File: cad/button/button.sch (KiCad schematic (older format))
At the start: 17 parts, among them J1 uSD_SPI, J2 SWD, SW1 SW_Push, U1 STM32L072KZTx, U2 PAM8302AAS

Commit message: more drawing
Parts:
- J1: footprint Connectors:microSD_Card_Receptacle_Wuerth_693072010801 -> custom:PJRC_uSD_Adapter
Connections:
- wire segments 59 -> 53
- no-connect marks 17 -> 16
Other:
- moved on the sheet: J1, J2
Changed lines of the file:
@@
 NoConn ~ 3250 3600
 NoConn ~ 3250 3700
-NoConn ~ 3250 4000
 NoConn ~ 2150 3100
 NoConn ~ 2150 3200
@@
 L Connector:Conn_01x04_Female J2
 U 1 1 5C3A9A62
-P 4100 4050
-F 0 "J2" H 4128 4026 50  0000 L CNN
-F 1 "SWD" H 4128 3935 50  0000 L CNN
-F 2 "custom:Pad_4contacts" H 4100 4050 50  0001 C CNN
-F 3 "~" H 4100 4050 50  0001 C CNN
-	1    4100 4050
+P 4100 3800
+F 0 "J2" H 4128 3776 50  0000 L CNN
+F 1 "SWD" H 4128 3685 50  0000 L CNN
+F 2 "custom:Pad_4contacts" H 4100 3800 50  0001 C CNN
+F 3 "~" H 4100 3800 50  0001 C CNN
+	1    4100 3800
 	1    0    0    -1
 $EndComp
@@
 L power:GND #PWR0101
 U 1 1 5C3AA417
-P 3900 4300
-F 0 "#PWR0101" H 3900 4050 50  0001 C CNN
-F 1 "GND" H 3905 4127 50  0000 C CNN
-F 2 "" H 3900 4300 50  0001 C CNN
-F 3 "" H 3900 4300 50  0001 C CNN
-	1    3900 4300
+P 3900 4050
+F 0 "#PWR0101" H 3900 3800 50  0001 C CNN
+F 1 "GND" H 3905 3877 50  0000 C CNN
+F 2 "" H 3900 4050 50  0001 C CNN
+F 3 "" H 3900 4050 50  0001 C CNN
+	1    3900 4050
 	1    0    0    -1
 $EndComp
@@
 L power:+3V3 #PWR0106
 U 1 1 5C3AA5DA
-P 3900 3900
-F 0 "#PWR0106" H 3900 3750 50  0001 C CNN
-F 1 "+3V3" H 3915 4073 50  0000 C CNN
-F 2 "" H 3900 3900 50  0001 C CNN
-F 3 "" H 3900 3900 50  0001 C CNN
-	1    3900 3900
+P 3900 3650
+F 0 "#PWR0106" H 3900 3500 50  0001 C CNN
+F 1 "+3V3" H 3915 3823 50  0000 C CNN
+F 2 "" H 3900 3650 50  0001 C CNN
+F 3 "" H 3900 3650 50  0001 C CNN
+	1    3900 3650
 	1    0    0    -1
 $EndComp
@@
 Text Label 1850 2700 0    50   ~ 0
 BOOT0
-Wire Wire Line
-	3250 3800 3600 3800
-Wire Wire Line
-	3250 3900 3550 3900
 $Comp
 L custom:uSD_SPI J1
 U 1 1 5C3DB7D2
-P 5950 3900
-F 0 "J1" H 5900 4617 50  0000 C CNN
-F 1 "uSD_SPI" H 5900 4526 50  0000 C CNN
-F 2 "Connectors:microSD_Card_Receptacle_Wuerth_693072010801" H 7100 4200 50  0001 C CNN
-F 3 "http://katalog.we-online.de/em/datasheet/693072010801.pdf" H 5950 3900 50  0001 C CNN
-	1    5950 3900
+P 5950 4150
+F 0 "J1" H 5900 4867 50  0000 C CNN
+F 1 "uSD_SPI" H 5900 4776 50  0000 C CNN
+F 2 "custom:PJRC_uSD_Adapter" H 7100 4450 50  0001 C CNN
+F 3 "http://katalog.we-online.de/em/datasheet/693072010801.pdf" H 5950 4150 50  0001 C CNN
+	1    5950 4150
 	1    0    0    -1
 $EndComp
@@
 Text GLabel 3250 2900 2    50   Input ~ 0
 SPK_IN
-Text GLabel 3250 3300 2    50   Input ~ 0
+Text GLabel 3250 4000 2    50   Input ~ 0
 SPK_SD
 Text GLabel 5100 2250 0    50   Input ~ 0
 SPK_IN
-Text GLabel 5050 3700 0    50   Input ~ 0
+Text GLabel 5050 4000 0    50   Input ~ 0
 SD_CS
-Text GLabel 5050 4000 0    50   Input ~ 0
+Text GLabel 5050 4100 0    50   Input ~ 0
 SD_SCK
+Text GLabel 5050 4300 0    50   Input ~ 0
+SD_MISO
 Text GLabel 5050 4200 0    50   Input ~ 0
-SD_MISO
-Text GLabel 5050 3800 0    50   Input ~ 0
 SD_MOSI
-Wire Wire Line
-	5050 3900 4550 3900
-Wire Wire Line
-	4550 3900 4550 3800
-Wire Wire Line
-	5050 4100 4550 4100
 $Comp
 L power:GND #PWR0115
 U 1 1 5C3DDAEF
-P 4550 4300
-F 0 "#PWR0115" H 4550 4050 50  0001 C CNN
-F 1 "GND" H 4555 4127 50  0000 C CNN
-F 2 "" H 4550 4300 50  0001 C CNN
-F 3 "" H 4550 4300 50  0001 C CNN
-	1    4550 4300
+P 5500 4900
+F 0 "#PWR0115" H 5500 4650 50  0001 C CNN
+F 1 "GND" H 5505 4727 50  0000 C CNN
+F 2 "" H 5500 4900 50  0001 C CNN
+F 3 "" H 5500 4900 50  0001 C CNN
+	1    5500 4900
 	1    0    0    -1
 $EndComp
@@
 L power:+3V3 #PWR0116
 U 1 1 5C3DDB14
-P 4550 3800
-F 0 "#PWR0116" H 4550 3650 50  0001 C CNN
-F 1 "+3V3" H 4565 3973 50  0000 C CNN
-F 2 "" H 4550 3800 50  0001 C CNN
-F 3 "" H 4550 3800 50  0001 C CNN
-	1    4550 3800
-	1    0    0    -1
-$EndComp
-NoConn ~ 6750 4500
+P 5500 3450
+F 0 "#PWR0116" H 5500 3300 50  0001 C CNN
+F 1 "+3V3" H 5515 3623 50  0000 C CNN
+F 2 "" H 5500 3450 50  0001 C CNN
+F 3 "" H 5500 3450 50  0001 C CNN
+	1    5500 3450
+	1    0    0    -1
+$EndComp
 Wire Wire Line
 	1450 2700 1450 2750
@@
 	2650 4250 2650 4300
 Wire Wire Line
-	3900 3900 3900 3950
-Wire Wire Line
-	3900 4250 3900 4300
-Wire Wire Line
-	3900 4150 3550 4150
-Wire Wire Line
-	3550 3900 3550 4150
-Wire Wire Line
-	3900 4050 3600 4050
-Wire Wire Line
-	3600 3800 3600 4050
-Wire Wire Line
-	4550 4100 4550 4300
+	3900 3650 3900 3700
+Wire Wire Line
+	3900 4000 3900 4050
+Wire Wire Line
+	5500 3450 5500 3500
+Wire Wire Line
+	5500 4850 5500 4900
+NoConn ~ 3250 3300
+Wire Wire Line
+	3250 3900 3900 3900
+Wire Wire Line
+	3250 3800 3900 3800
 $EndSCHEMATC

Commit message: finish up schematic
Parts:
- removed C2: 1uF, Capacitors_SMD:C_0603_HandSoldering, symbol Device:CP_Small
- removed C3: 10uF, Capacitors_SMD:C_0603_HandSoldering, symbol Device:CP_Small
- removed C6: 100nF, Capacitors_SMD:C_0603_HandSoldering, symbol Device:C_Small
- added C1, C2, C9: 10uF, Capacitors_SMD:C_0603_HandSoldering, symbol Device:C_Small
- added C10, C11: 220pF, Capacitors_SMD:C_0603_HandSoldering, symbol Device:C_Small
- added C5, C7, C8: 1uF, Capacitors_SMD:C_0603_HandSoldering, symbol Device:C_Small
- added FB1, FB2: Ferrite_Bead_Small, Resistors_SMD:R_0603_HandSoldering, symbol Device:Ferrite_Bead_Small
- added Q1: DMC2038LVT, TO_SOT_Packages_SMD:TSOT-23-6, symbol custom:DMC2038LVT
- added R1, R6, R7: 10K, Resistors_SMD:R_0603_HandSoldering, symbol Device:R_Small
- added R4: 10, Resistors_SMD:R_0603_HandSoldering, symbol Device:R_Small
- added RV1: R_POT, Potentiometers:Potentiometer_Trimmer-EVM3E, symbol Device:R_POT
- R2: value 1K -> 10K
- R3: value 10K -> not fitted
- SW1: value SW_Push -> Button
- renumbered C4 to C3, C5 to C4, C1 to C6, R1 to R5, R4 to R8
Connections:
- net +3V3: now also R3.1, R8.1, C2.1, C9.2, Q1.6 (D), R4.1; no longer BT1.1 (+), C6.2, SW1.2, U1.5 (VDDA)
- net GND: now also R2.2, SW1.2, C1.2, C10.2, C11.2, C2.2, C5.1, C9.1, Q1.4 (D); no longer R3.2, R8.1, U2.4 (IN-)
- net SD_CS: now also U1.25 (PA15); no longer U1.14 (PB0)
- net SD_MISO: now also U1.27 (PB4); no longer U1.12 (PA6)
- net SD_MOSI: now also U1.28 (PB5); no longer U1.13 (PA7)
- net SD_SCK: now also U1.26 (PB3); no longer U1.11 (PA5)
- net SPK_SD: now also U1.22 (PA12); no longer U1.25 (PA15)
- net SPK_1: no longer names the net of U2.5 (OUT+)
- net SPK_1: now also FB1.1; no longer LS1.1
- net SPK_2: no longer names the net of U2.8 (OUT-)
- net SPK_2: now also FB2.1; no longer LS1.2
- net SPK_IN: no longer names the net of U2.3 (IN+)
- net SPK_IN: now also R6.1; no longer U1.10 (PA4)
- net SW_IN: no longer names the net of U1.6 (PA0)
- net SW_IN: no longer R2.2
- new net: R7.1, U2.4 (IN-)
- new net: C7.2, RV1.2
- new net: C7.1, R6.2
- new net: C8.1, R7.2
- new net GATE_N: Q1.1 (G), Q1.2 (S), R1.1, SW1.1
- new net GATE_P: Q1.3 (G), R2.1, R3.2
- new net SPK+: C11.1, FB1.2, LS1.1
- new net SPK-: C10.1, FB2.2, LS1.2
- new net SPK_IN+: RV1.3, U1.10 (PA4)
- new net SPK_IN-: C8.2, RV1.1, U1.11 (PA5)
- new net VBAT: BT1.1 (+), C1.1, Q1.5 (S), R1.2
- new net VDDA: C5.2, C6.2, R4.2, U1.5 (VDDA)
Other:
- note added: "Audio amplifier"
- note added: "Battery and power-on switch"
- note added: "MCU and programming header"
- note added: "SD card adapter"
- moved on the sheet: BT1, C3, C4, C6, J1, J2, LS1, R5, R8, SW1, U1, U2

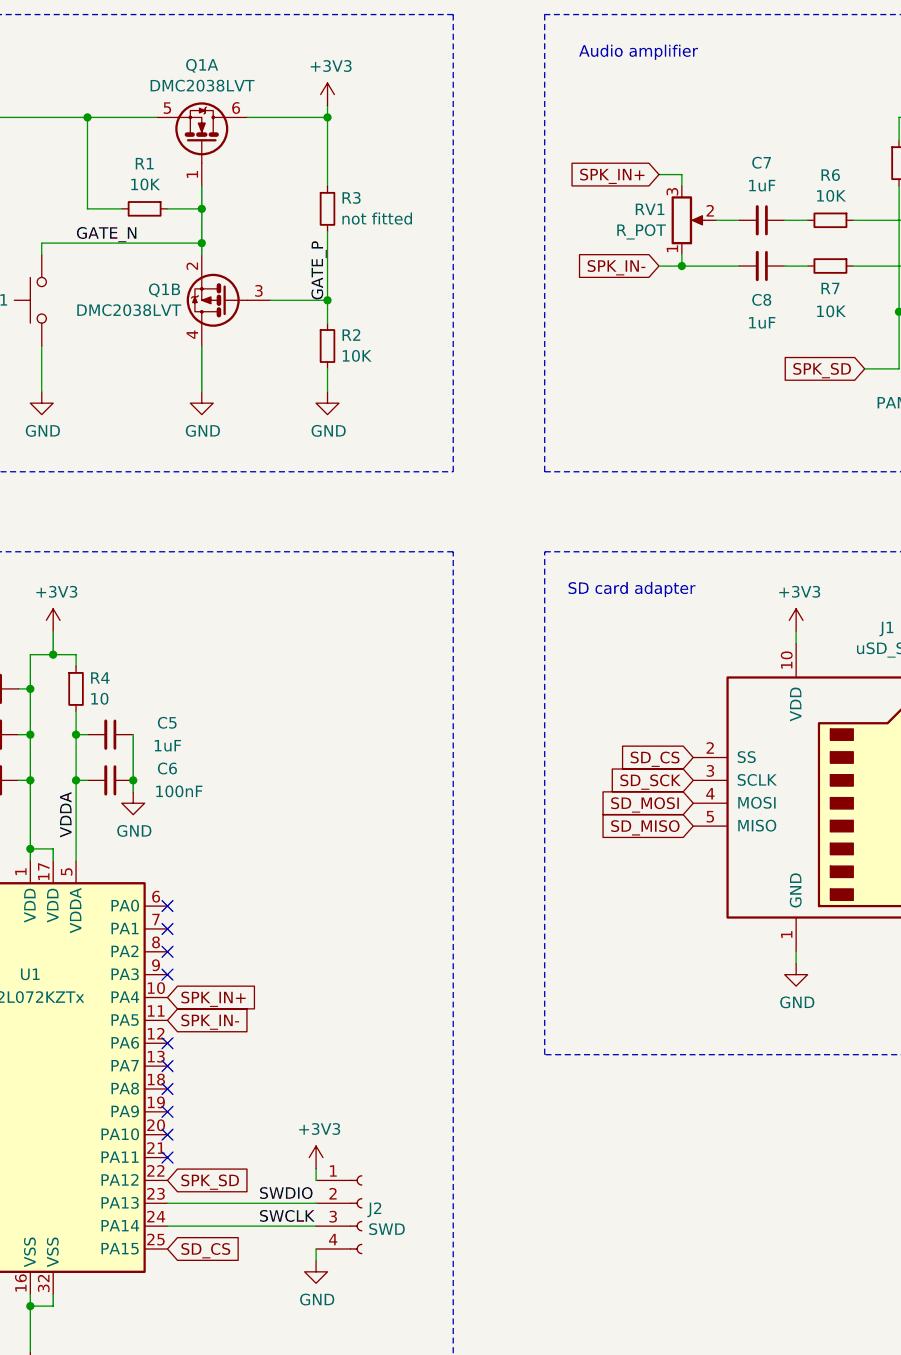
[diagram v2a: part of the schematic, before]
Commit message: move STM to below sdcard
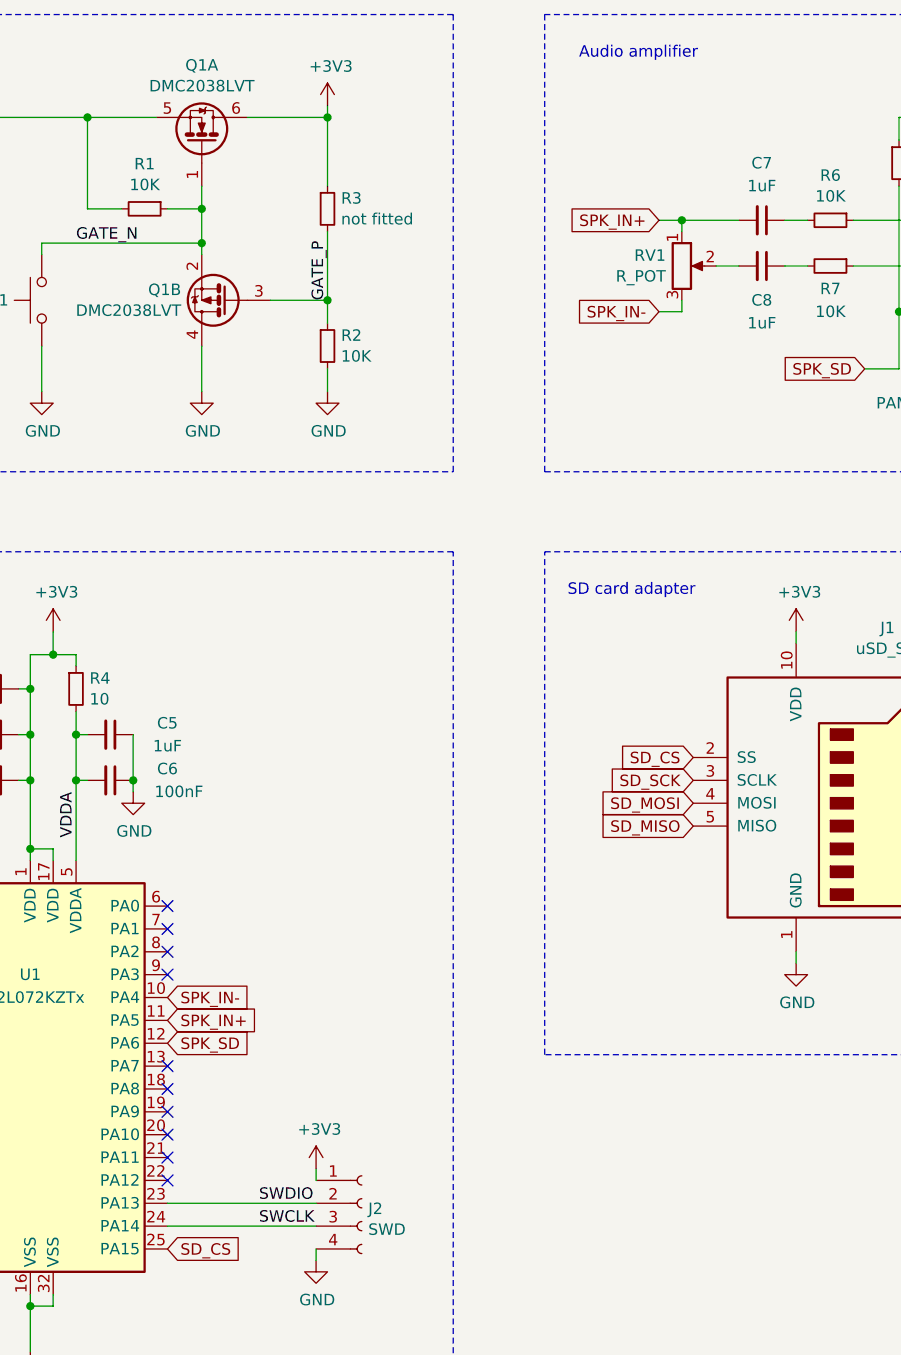
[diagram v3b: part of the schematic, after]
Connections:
- net SPK_IN+: now also C7.2, RV1.1, U1.11 (PA5); no longer RV1.3, U1.10 (PA4)
- net SPK_IN-: now also RV1.3, U1.10 (PA4); no longer C8.2, RV1.1, U1.11 (PA5)
- net SPK_SD: now also U1.12 (PA6); no longer U1.22 (PA12)
- net at RV1.2: now also C8.2; no longer C7.2
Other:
- moved on the sheet: RV1
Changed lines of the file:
@@
 Text GLabel 3600 6600 2    50   Input ~ 0
 SD_CS
-Text GLabel 3600 5500 2    50   Input ~ 0
+Text GLabel 3600 5600 2    50   Input ~ 0
 SPK_IN+
-Text GLabel 3600 6300 2    50   Input ~ 0
+Text GLabel 3600 5700 2    50   Input ~ 0
 SPK_SD
-Text GLabel 5750 1900 0    50   Input ~ 0
+Text GLabel 5750 2100 0    50   Input ~ 0
 SPK_IN+
 Text GLabel 5900 4450 0    50   Input ~ 0
@@
 Wire Wire Line
 	3000 6850 3000 7050
-Text GLabel 3600 5600 2    50   Input ~ 0
+Text GLabel 3600 5500 2    50   Input ~ 0
 SPK_IN-
-Text GLabel 5750 2300 0    50   Input ~ 0
+Text GLabel 5750 2500 0    50   Input ~ 0
 SPK_IN-
 $Comp
@@
 L Device:R_POT RV1
 U 1 1 5C3FAFD1
-P 5850 2100
-F 0 "RV1" H 5780 2054 50  0000 R CNN
-F 1 "R_POT" H 5780 2145 50  0000 R CNN
-F 2 "Potentiometers:Potentiometer_Trimmer-EVM3E" H 5850 2100 50  0001 C CNN
-F 3 "~" H 5850 2100 50  0001 C CNN
-	1    5850 2100
-	1    0    0    1
+P 5850 2300
+F 0 "RV1" H 5780 2346 50  0000 R CNN
+F 1 "R_POT" H 5780 2255 50  0000 R CNN
+F 2 "Potentiometers:Potentiometer_Trimmer-EVM3E" H 5850 2300 50  0001 C CNN
+F 3 "~" H 5850 2300 50  0001 C CNN
+	1    5850 2300
+	1    0    0    -1
 $EndComp
 $Comp
@@
 	0    1    1    0
 $EndComp
-Wire Wire Line
-	6000 2100 6100 2100
 $Comp
 L Device:R_Small R6
@@
 	0    1    1    0
 $EndComp
-Wire Wire Line
-	5750 2300 5850 2300
-Wire Wire Line
-	5850 2250 5850 2300
-Connection ~ 5850 2300
-Wire Wire Line
-	5850 2300 6100 2300
-Wire Wire Line
-	5750 1900 5850 1900
-Wire Wire Line
-	5850 1900 5850 1950
 Wire Wire Line
 	6650 2750 6800 2750
@@
 Text Label 4300 2450 1    50   ~ 0
 GATE_P
-NoConn ~ 3600 5700
+NoConn ~ 3600 6300
+Wire Wire Line
+	6000 2300 6100 2300
+Wire Wire Line
+	5750 2500 5850 2500
+Wire Wire Line
+	5850 2500 5850 2450
+Wire Wire Line
+	5850 2150 5850 2100
+Wire Wire Line
+	5850 2100 5750 2100
+Wire Wire Line
+	5850 2100 6100 2100
+Connection ~ 5850 2100
 $EndSCHEMATC

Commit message: update with help from Enno
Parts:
- added R6: 1K, Resistors_SMD:R_0603_HandSoldering, symbol Device:R_Small
- SW1: footprint Buttons_Switches_THT:SW_PUSH-12mm -> custom:SW_PUSH-12mm
- renumbered R6 to R7, R7 to R8, R8 to R9
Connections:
- net +3V3: now also Q1.4 (D); no longer Q1.6 (D), R9.1
- net GND: now also Q1.5 (S), R9.2; no longer Q1.4 (D), SW1.2
- net SPK_SD: now also R9.1; no longer R9.2
- net VBAT: now also Q1.2 (S), SW1.1; no longer Q1.5 (S)
- net at U1.6 (PA0): now also R6.2
- removed net GATE_N: Q1.1 (G), Q1.2 (S), R1.1, SW1.1
- net GATE_P renamed POWERON
- net POWERON: now also Q1.1 (G), SW1.2, R6.1; no longer Q1.3 (G)
- new net: Q1.3 (G), Q1.6 (D), R1.1
- no-connect marks 16 -> 15
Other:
- moved on the sheet: BT1, C1, C10, C11, C7, C8, C9, FB1, FB2, LS1, Q1A, Q1B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

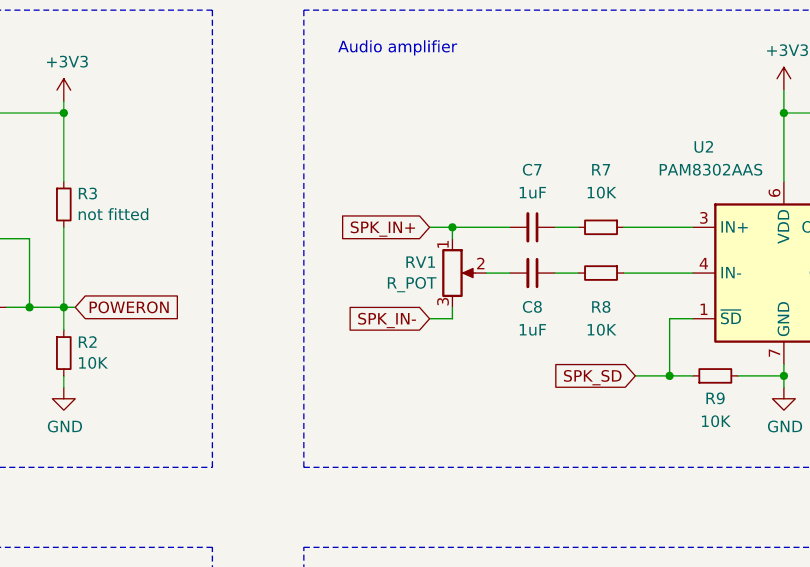
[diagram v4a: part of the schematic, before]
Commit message: update Pot footprint
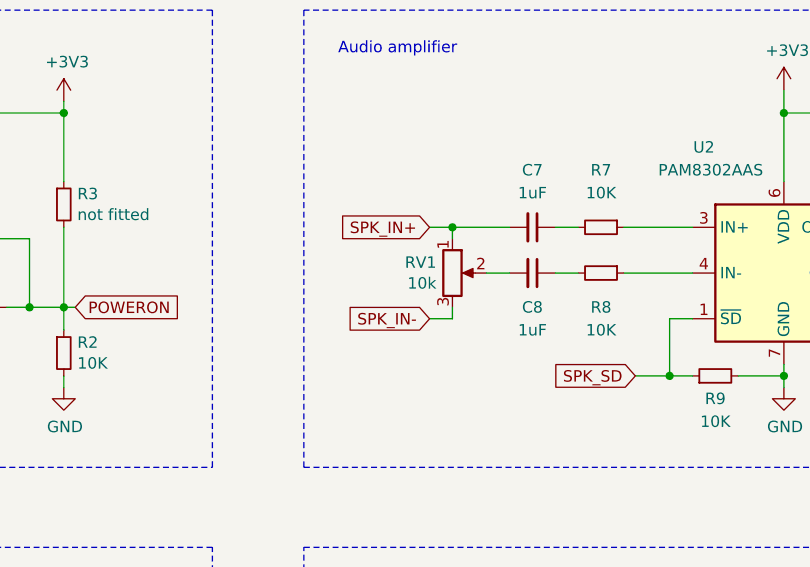
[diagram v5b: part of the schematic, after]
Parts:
- RV1: value R_POT -> 10k; footprint Potentiometers:Potentiometer_Trimmer-EVM3E -> custom:Potentiometer_Trimmer-EVM3Y
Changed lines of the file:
@@
 P 5900 2350
 F 0 "RV1" H 5830 2396 50  0000 R CNN
-F 1 "R_POT" H 5830 2305 50  0000 R CNN
-F 2 "Potentiometers:Potentiometer_Trimmer-EVM3E" H 5900 2350 50  0001 C CNN
+F 1 "10k" H 5830 2305 50  0000 R CNN
+F 2 "custom:Potentiometer_Trimmer-EVM3Y" H 5900 2350 50  0001 C CNN
 F 3 "~" H 5900 2350 50  0001 C CNN
 	1    5900 2350

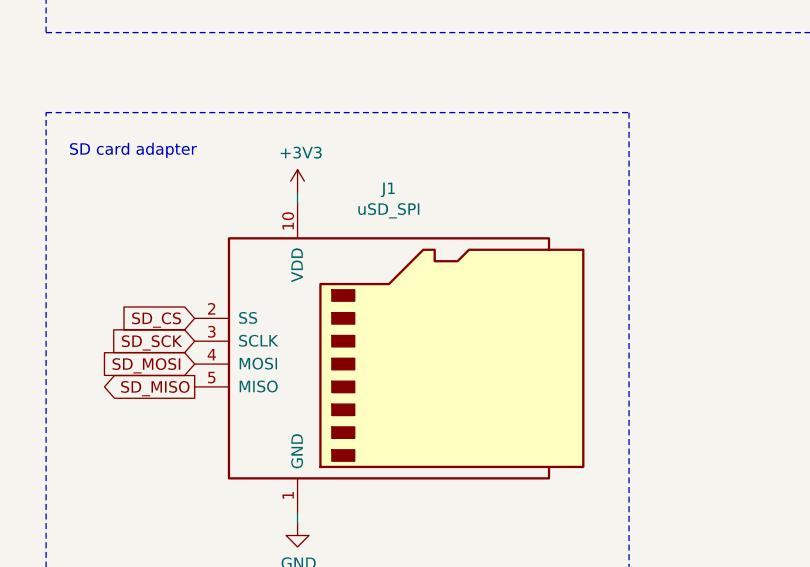
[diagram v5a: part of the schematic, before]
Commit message: prepare for other sdcard adapter
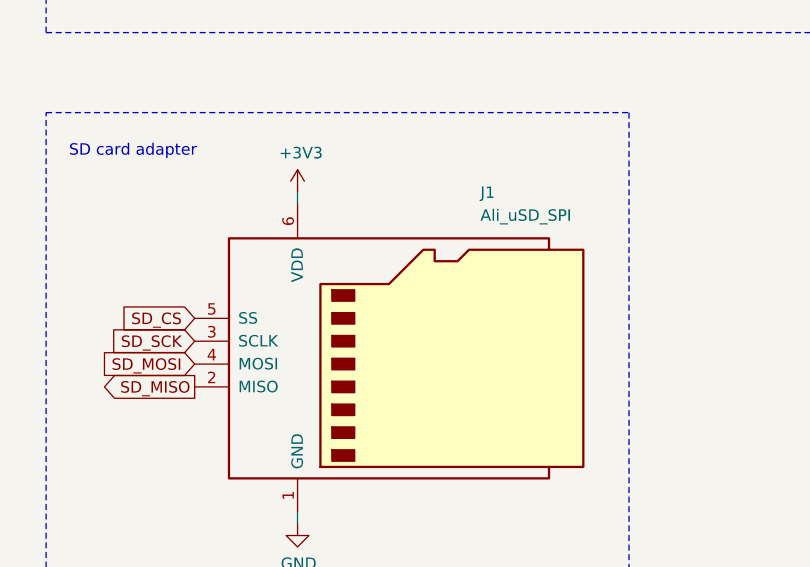
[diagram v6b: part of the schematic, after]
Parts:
- removed J1: uSD_SPI, custom:PJRC_uSD_Adapter, symbol custom:uSD_SPI
- added J1: Ali_uSD_SPI, custom:Ali_uSD_Adapter, symbol custom:Ali_uSD_SPI
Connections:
- net +3V3: now also J1.6 (VDD)
- net GND: now also J1.1 (GND)
- net SD_CS: now also J1.5 (SS)
- net SD_MISO: now also J1.2 (MISO)
- net SD_MOSI: now also J1.4 (MOSI)
- net SD_SCK: now also J1.3 (SCLK)
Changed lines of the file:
@@
 Text Label 2200 5300 0    50   ~ 0
 BOOT0
-$Comp
-L custom:uSD_SPI J1
-U 1 1 5C3DB7D2
-P 6800 4600
-F 0 "J1" H 6750 5317 50  0000 C CNN
-F 1 "uSD_SPI" H 6750 5226 50  0000 C CNN
-F 2 "custom:PJRC_uSD_Adapter" H 7950 4900 50  0001 C CNN
-F 3 "http://katalog.we-online.de/em/datasheet/693072010801.pdf" H 6800 4600 50  0001 C CNN
-	1    6800 4600
-	1    0    0    -1
-$EndComp
 Text GLabel 2450 6200 0    50   Output ~ 0
 SD_SCK
@@
 Wire Wire Line
 	7700 1650 7850 1650
+$Comp
+L custom:Ali_uSD_SPI J1
+U 1 1 5C452F0C
+P 6800 4600
+F 0 "J1" H 7150 5300 50  0000 L CNN
+F 1 "Ali_uSD_SPI" H 7150 5200 50  0000 L CNN
+F 2 "custom:Ali_uSD_Adapter" H 7950 4850 50  0001 C CNN
+F 3 "http://katalog.we-online.de/em/datasheet/693072010801.pdf" H 6800 4550 50  0001 C CNN
+	1    6800 4600
+	1    0    0    -1
+$EndComp
 $EndSCHEMATC
